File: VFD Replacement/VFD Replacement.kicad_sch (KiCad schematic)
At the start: 5 parts, among them J1 Conn_01x05_Pin, J2 Conn_01x05_Pin, J3 Conn_01x06_Pin, J4 Conn_01x06_Pin, J5 Conn_01x02_Pin

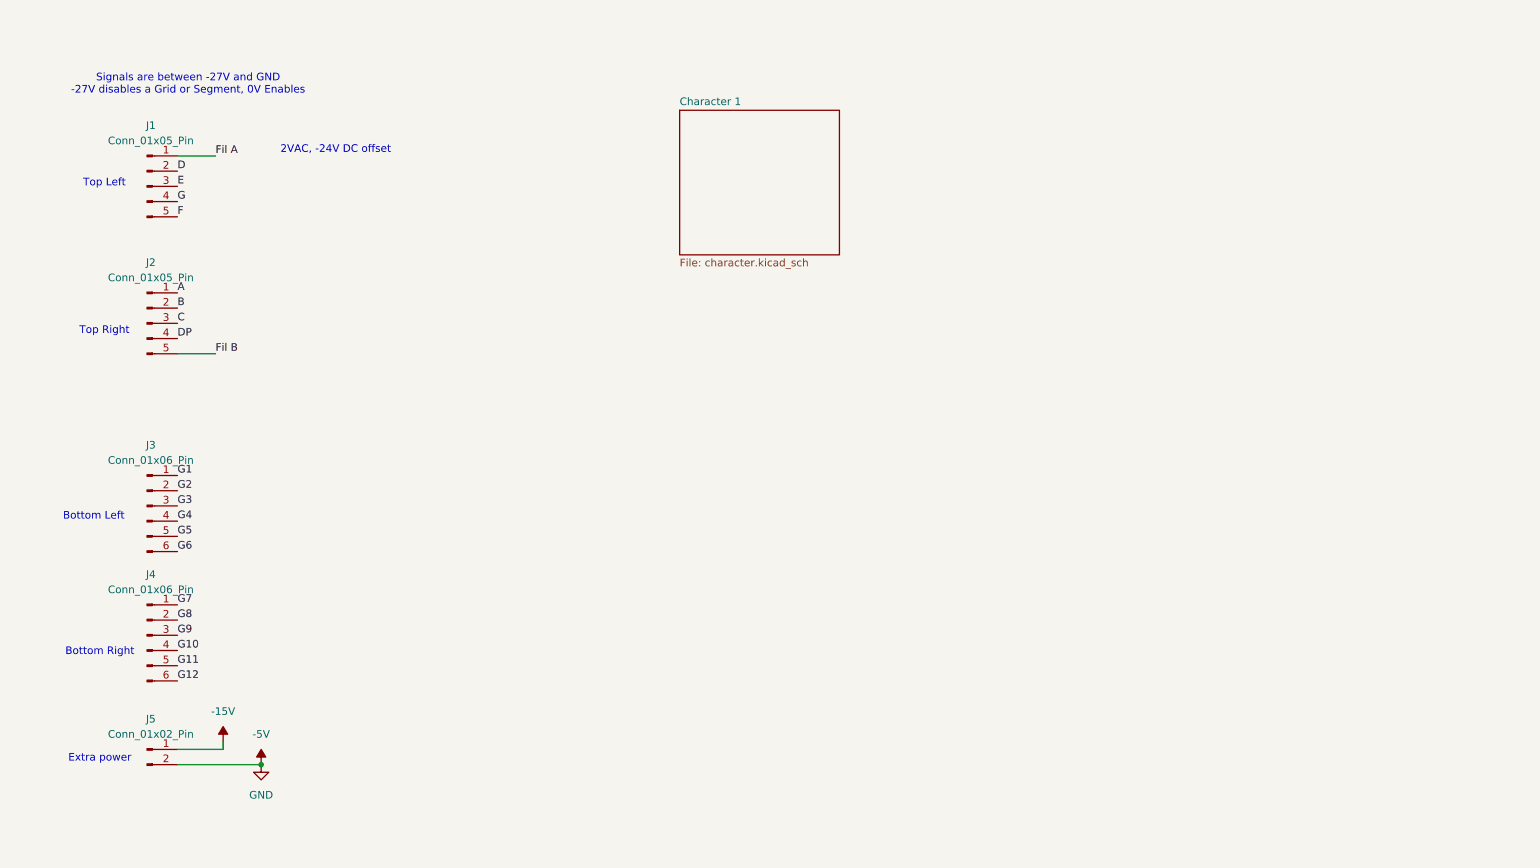
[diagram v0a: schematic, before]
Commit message: Create Display PCB
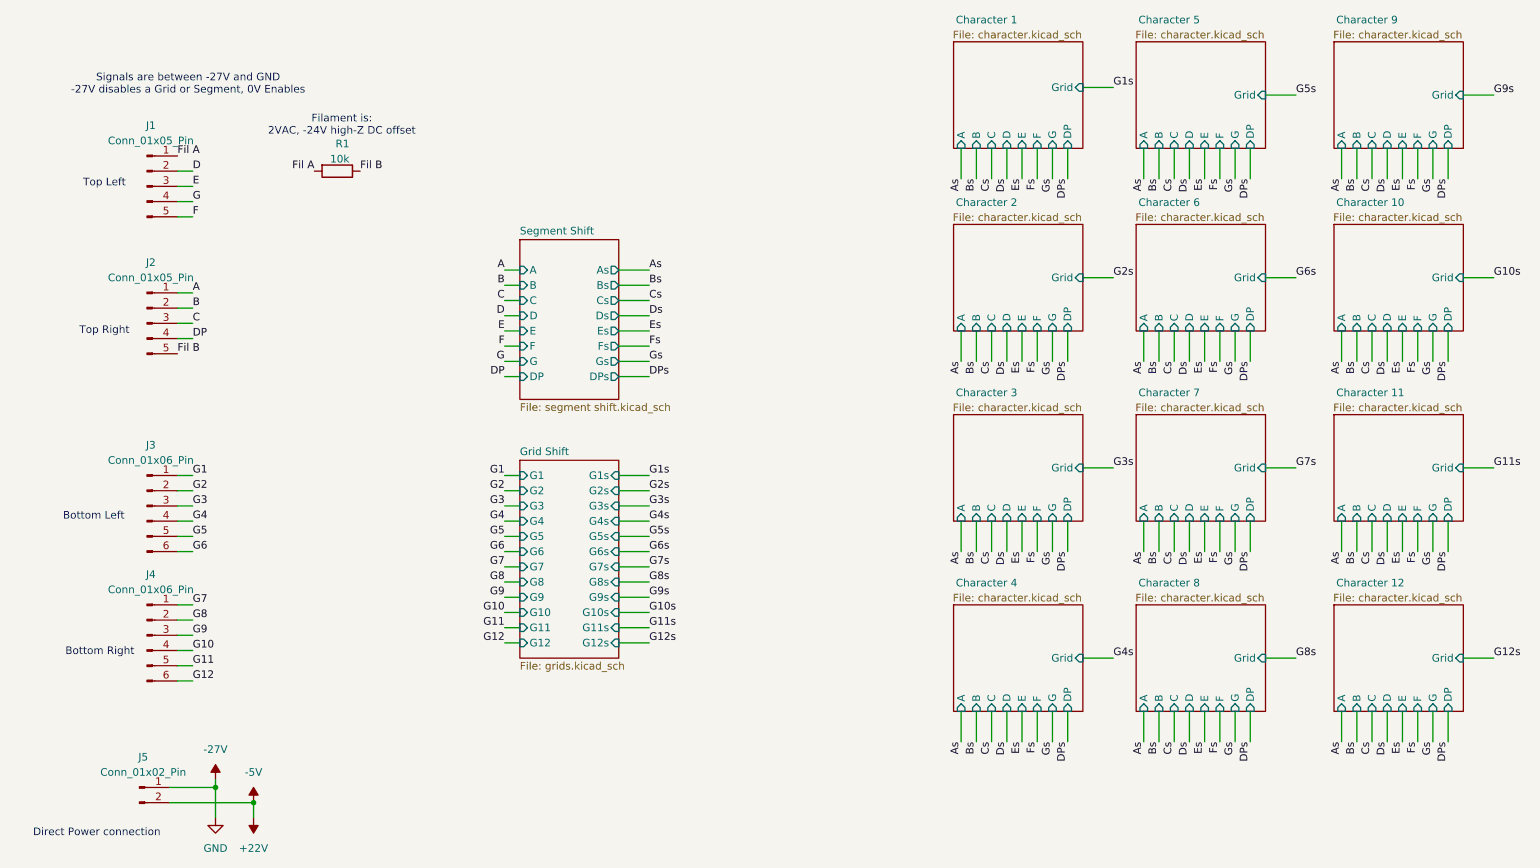
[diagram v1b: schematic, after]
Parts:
- added R1: 10k, Resistor_SMD:R_0603_1608Metric_Pad0.98x0.95mm_HandSolder, symbol Device:R
- J1, J2: footprint (none) -> footprints:Conn_1x05 2.5mm
- J3, J4: footprint (none) -> footprints:Conn_1x06 2.5mm
- J5: footprint (none) -> Connector_PinHeader_2.54mm:PinHeader_1x02_P2.54mm_Vertical
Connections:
- net Fil A: now also R1.2
- net Fil B: now also R1.1
- net -15V renamed -27V
- net -5V renamed +22V
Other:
- added sheet Character 10 (character.kicad_sch)
- added sheet Character 11 (character.kicad_sch)
- added sheet Character 12 (character.kicad_sch)
- added sheet Character 2 (character.kicad_sch)
- added sheet Character 3 (character.kicad_sch)
- added sheet Character 4 (character.kicad_sch)
- added sheet Character 5 (character.kicad_sch)
- added sheet Character 6 (character.kicad_sch)
- added sheet Character 7 (character.kicad_sch)
- added sheet Character 8 (character.kicad_sch)
- added sheet Character 9 (character.kicad_sch)
- added sheet Grid Shift (grids.kicad_sch)
- added sheet Segment Shift (segment shift.kicad_sch)
- sheet Character 1 ports: added A, B, C, D, DP, E, F, G, Grid; removed none
- note added: "Direct Power connection"
- note added: "Filament is: 2VAC, -24V high-Z DC offset"
- note removed: "2VAC, -24V DC offset"
- note removed: "Extra power"
- moved on the sheet: J5

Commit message: Complete
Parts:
- added U1: ~, footprints:display, symbol project parts:display
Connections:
- net As: now also U1.5 (A)
- net Bs: now also U1.6 (B)
- net Cs: now also U1.7 (C)
- net DPs: now also U1.8 (DP)
- net Ds: now also U1.1 (D)
- net Es: now also U1.2 (E)
- net Fs: now also U1.4 (F)
- net G10s: now also U1.18 (G10)
- net G11s: now also U1.19 (G11)
- net G12s: now also U1.20 (G12)
- net G1s: now also U1.9 (G1)
- net G2s: now also U1.10 (G2)
- net G3s: now also U1.11 (G3)
- net G4s: now also U1.12 (G4)
- net G5s: now also U1.13 (G5)
- net G6s: now also U1.14 (G6)
- net G7s: now also U1.15 (G7)
- net G8s: now also U1.16 (G8)
- net G9s: now also U1.17 (G9)
- net Gs: now also U1.3 (G)
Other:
- removed sheet Character 1
- removed sheet Character 10
- removed sheet Character 11
- removed sheet Character 12
- removed sheet Character 2
- removed sheet Character 3
- removed sheet Character 4
- removed sheet Character 5
- removed sheet Character 6
- removed sheet Character 7
- removed sheet Character 8
- removed sheet Character 9

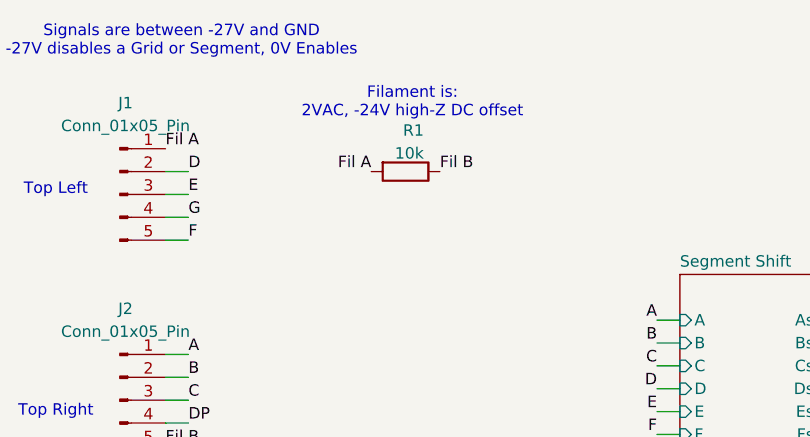
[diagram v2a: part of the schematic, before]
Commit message: Update values from sim
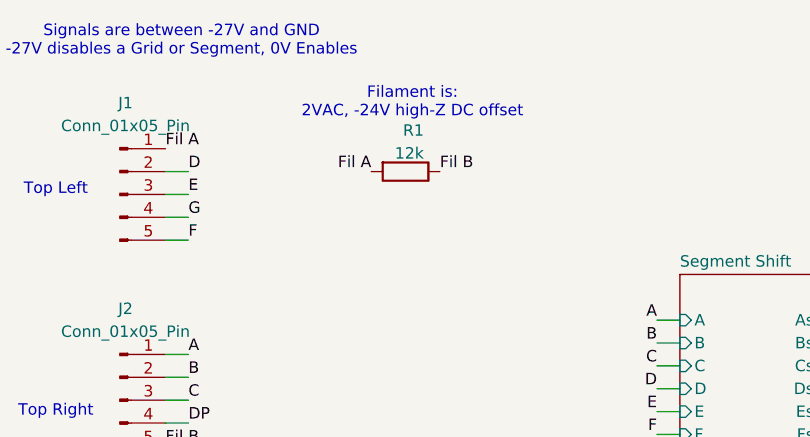
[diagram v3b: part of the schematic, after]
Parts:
- R1: value 10k -> 12k
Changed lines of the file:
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@@
       (effects (font (size 1.27 1.27)) (justify right))
     )
-    (property "Value" "10k" (at 83.312 44.958 90)
+    (property "Value" "12k" (at 83.312 44.958 90)
       (effects (font (size 1.27 1.27)) (justify right))
     )
